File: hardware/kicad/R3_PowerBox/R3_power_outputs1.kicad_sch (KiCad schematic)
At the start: 12 parts, among them J10 BATTERY / CHARGER TELEMETRY, J11 USER PANEL / PRIMARY ONLY, J12 PRIMARY B2B 2x8 / DNP, J13 ISOLATED B2B 2x5 / DNP, J2 DIGITAL POWER OUT, J3 ISOLATED POWER OUT, J4 CONTROL / SERVICE, J5 PRIMARY AUX DNP, J6 ISOLATED AUX DNP

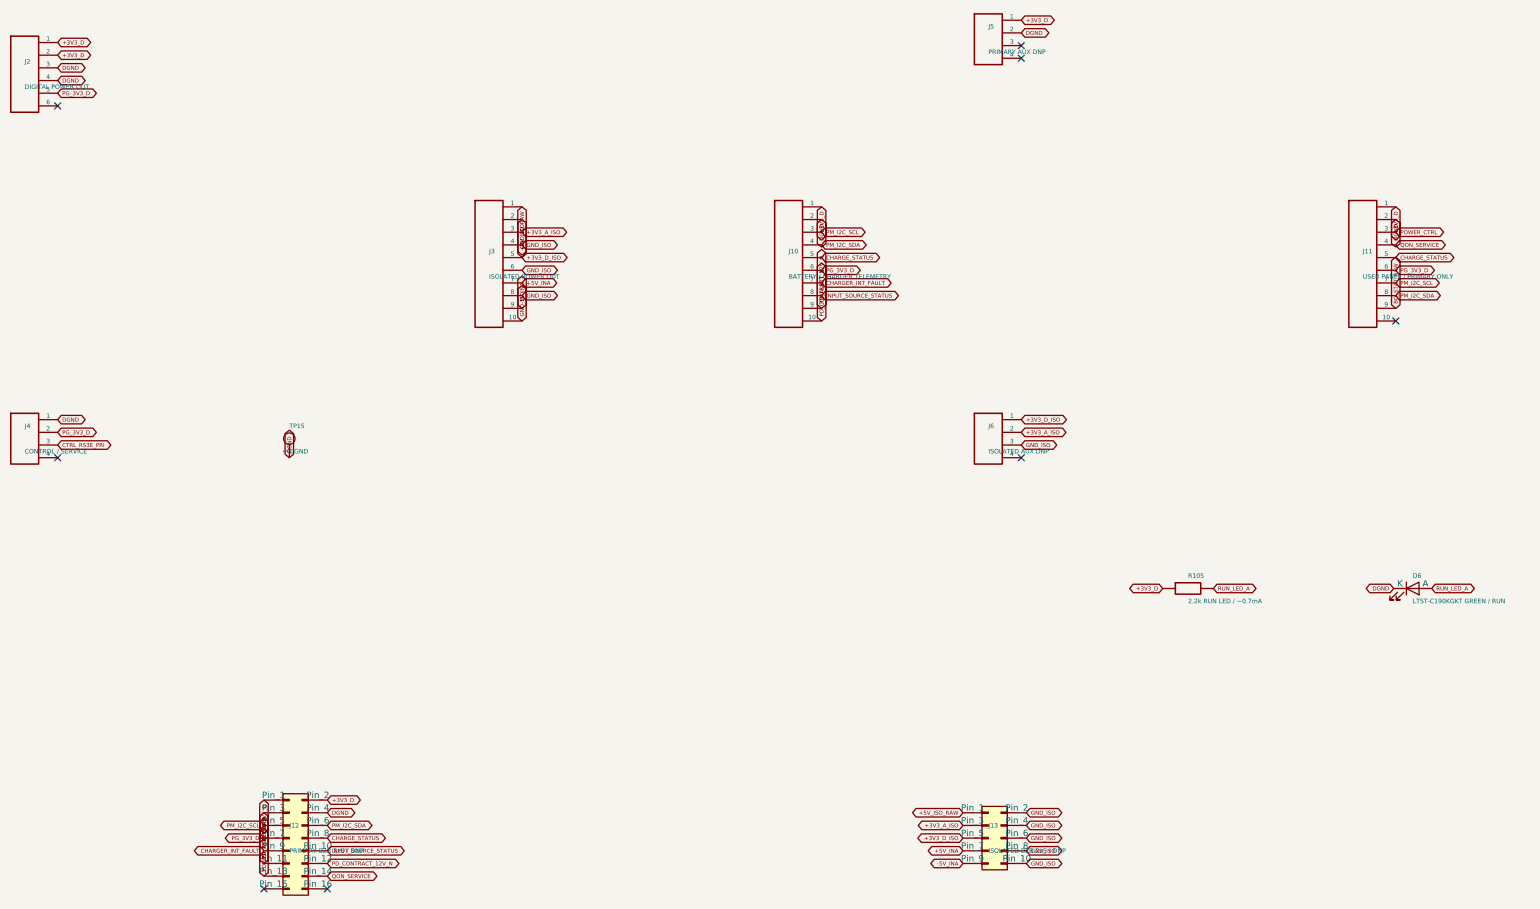
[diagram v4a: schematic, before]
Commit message: Finish R3 PowerBox routing checkpoint F and verification
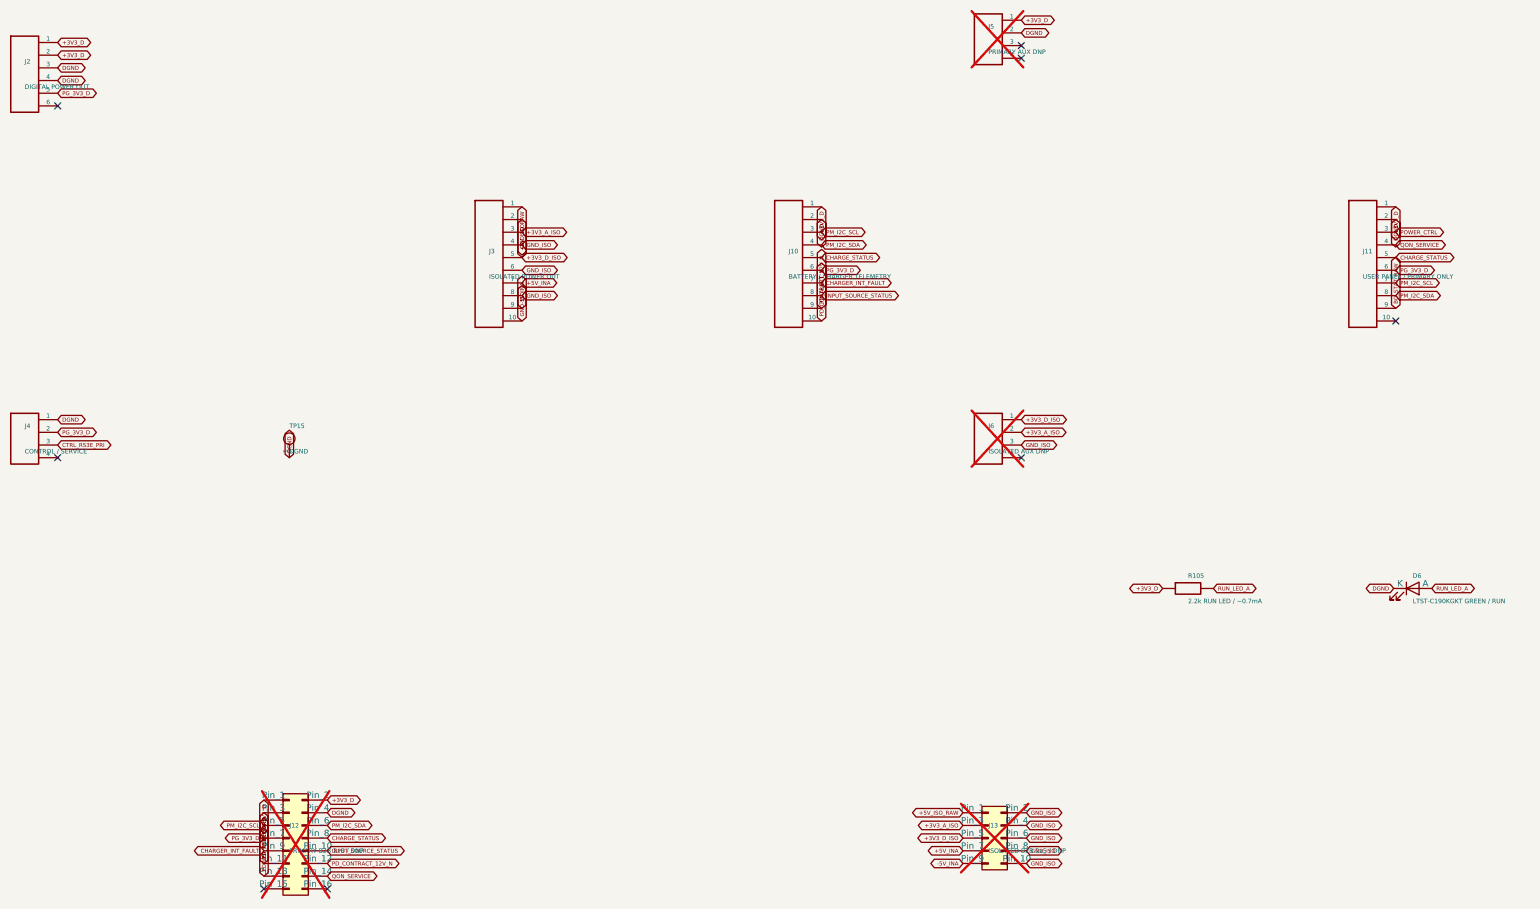
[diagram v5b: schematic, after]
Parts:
- J12, J13, J5, J6: now not fitted
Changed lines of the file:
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@@
     (instances
       (project "SKiDL-Generated"
-        (path "/9be6bff1-dc85-4a48-94a9-d7223c5e518f/8a113b12-9d71-5245-be88-2275cf0b9c69"
+        (path "/c950aac3-a7f8-40a1-8854-63ca2e6194cc/8a113b12-9d71-5245-be88-2275cf0b9c69"
           (reference "J2")
           (unit 1)))))
@@
     (instances
       (project "SKiDL-Generated"
-        (path "/9be6bff1-dc85-4a48-94a9-d7223c5e518f/8a113b12-9d71-5245-be88-2275cf0b9c69"
+        (path "/c950aac3-a7f8-40a1-8854-63ca2e6194cc/8a113b12-9d71-5245-be88-2275cf0b9c69"
           (reference "J3")
           (unit 1)))))
@@
     (instances
       (project "SKiDL-Generated"
-        (path "/9be6bff1-dc85-4a48-94a9-d7223c5e518f/8a113b12-9d71-5245-be88-2275cf0b9c69"
+        (path "/c950aac3-a7f8-40a1-8854-63ca2e6194cc/8a113b12-9d71-5245-be88-2275cf0b9c69"
           (reference "J4")
           (unit 1)))))
@@
     (in_bom yes)
     (on_board yes)
-    (dnp no)
+    (dnp yes)
     (fields_autoplaced yes)
     (property "Reference" "J5"
@@
     (instances
       (project "SKiDL-Generated"
-        (path "/9be6bff1-dc85-4a48-94a9-d7223c5e518f/8a113b12-9d71-5245-be88-2275cf0b9c69"
+        (path "/c950aac3-a7f8-40a1-8854-63ca2e6194cc/8a113b12-9d71-5245-be88-2275cf0b9c69"
           (reference "J5")
           (unit 1)))))
@@
     (in_bom yes)
     (on_board yes)
-    (dnp no)
+    (dnp yes)
     (fields_autoplaced yes)
     (property "Reference" "J6"
@@
     (instances
       (project "SKiDL-Generated"
-        (path "/9be6bff1-dc85-4a48-94a9-d7223c5e518f/8a113b12-9d71-5245-be88-2275cf0b9c69"
+        (path "/c950aac3-a7f8-40a1-8854-63ca2e6194cc/8a113b12-9d71-5245-be88-2275cf0b9c69"
           (reference "J6")
           (unit 1)))))
@@
     (instances
       (project "SKiDL-Generated"
-        (path "/9be6bff1-dc85-4a48-94a9-d7223c5e518f/8a113b12-9d71-5245-be88-2275cf0b9c69"
+        (path "/c950aac3-a7f8-40a1-8854-63ca2e6194cc/8a113b12-9d71-5245-be88-2275cf0b9c69"
           (reference "J10")
           (unit 1)))))
@@
     (instances
       (project "SKiDL-Generated"
-        (path "/9be6bff1-dc85-4a48-94a9-d7223c5e518f/8a113b12-9d71-5245-be88-2275cf0b9c69"
+        (path "/c950aac3-a7f8-40a1-8854-63ca2e6194cc/8a113b12-9d71-5245-be88-2275cf0b9c69"
           (reference "J11")
           (unit 1)))))
@@
     (in_bom yes)
     (on_board yes)
-    (dnp no)
+    (dnp yes)
     (fields_autoplaced yes)
     (property "Reference" "J12"
@@
     (instances
       (project "SKiDL-Generated"
-        (path "/9be6bff1-dc85-4a48-94a9-d7223c5e518f/8a113b12-9d71-5245-be88-2275cf0b9c69"
+        (path "/c950aac3-a7f8-40a1-8854-63ca2e6194cc/8a113b12-9d71-5245-be88-2275cf0b9c69"
           (reference "J12")
           (unit 1)))))
@@
     (in_bom yes)
     (on_board yes)
-    (dnp no)
+    (dnp yes)
     (fields_autoplaced yes)
     (property "Reference" "J13"
@@
     (instances
       (project "SKiDL-Generated"
-        (path "/9be6bff1-dc85-4a48-94a9-d7223c5e518f/8a113b12-9d71-5245-be88-2275cf0b9c69"
+        (path "/c950aac3-a7f8-40a1-8854-63ca2e6194cc/8a113b12-9d71-5245-be88-2275cf0b9c69"
           (reference "J13")
           (unit 1)))))
@@
     (instances
       (project "SKiDL-Generated"
-        (path "/9be6bff1-dc85-4a48-94a9-d7223c5e518f/8a113b12-9d71-5245-be88-2275cf0b9c69"
+        (path "/c950aac3-a7f8-40a1-8854-63ca2e6194cc/8a113b12-9d71-5245-be88-2275cf0b9c69"
           (reference "R105")
           (unit 1)))))
@@
     (instances
       (project "SKiDL-Generated"
-        (path "/9be6bff1-dc85-4a48-94a9-d7223c5e518f/8a113b12-9d71-5245-be88-2275cf0b9c69"
+        (path "/c950aac3-a7f8-40a1-8854-63ca2e6194cc/8a113b12-9d71-5245-be88-2275cf0b9c69"
           (reference "D6")
           (unit 1)))))
@@
     (instances
       (project "SKiDL-Generated"
-        (path "/9be6bff1-dc85-4a48-94a9-d7223c5e518f/8a113b12-9d71-5245-be88-2275cf0b9c69"
+        (path "/c950aac3-a7f8-40a1-8854-63ca2e6194cc/8a113b12-9d71-5245-be88-2275cf0b9c69"
           (reference "TP15")
           (unit 1)))))
